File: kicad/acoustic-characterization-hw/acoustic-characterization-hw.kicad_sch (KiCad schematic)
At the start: 0 parts

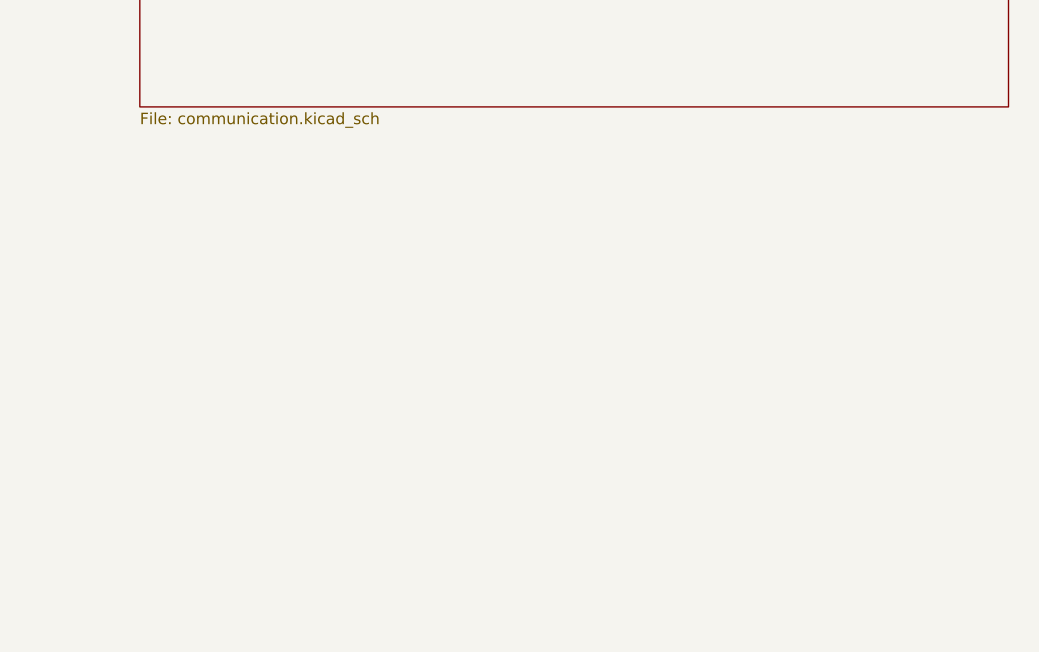
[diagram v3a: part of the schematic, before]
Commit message: [kicad] Chose RAM, connecting pins
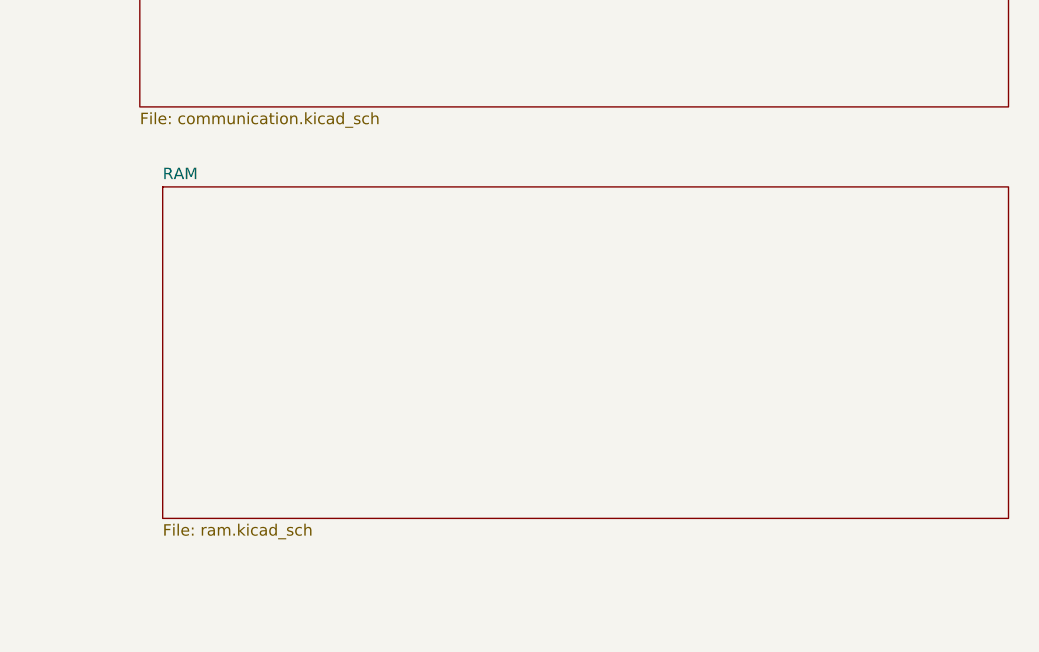
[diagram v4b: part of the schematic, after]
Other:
- added sheet RAM (ram.kicad_sch)
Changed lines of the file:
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@@
+		)
+	)
+	(sheet
+		(at 177.8 123.19)
+		(size 93.98 36.83)
+		(exclude_from_sim no)
+		(in_bom yes)
+		(on_board yes)
+		(dnp no)
+		(fields_autoplaced yes)
+		(stroke
+			(width 0.1524)
+			(type solid)
+		)
+		(fill
+			(color 0 0 0 0.0000)
+		)
+		(property "Sheetname" "RAM"
+			(at 177.8 122.4784 0)
+			(effects
+				(font
+					(size 1.27 1.27)
+				)
+				(justify left bottom)
+			)
+		)
+		(property "Sheetfile" "ram.kicad_sch"
+			(at 177.8 160.6046 0)
+			(effects
+				(font
+					(size 1.27 1.27)
+				)
+				(justify left top)
+			)
+		)
+		(property "Field2" ""
+			(at 177.8 123.19 0)
+			(effects
+				(font
+					(size 1.27 1.27)
+				)
+			)
+		)
+		(instances
+			(project "acoustic-characterization-hw"
+				(path "/25b015c9-ab13-4427-b72c-b6f348597100"
+					(page "7")
+				)
+			)
 		)
 	)
